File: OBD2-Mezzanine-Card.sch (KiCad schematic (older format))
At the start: 59 parts, among them P1 CONN_02X20

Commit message: sch: Add the 12volt power supply
Also rearrange a bit more

Signed-off-by: Alistair Francis <alistair@alistair23.me>
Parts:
- added D?: D, symbol D
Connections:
- net labels added: V12
- net labels removed: +12V
- wire segments 185 -> 183
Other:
- moved on the sheet: C?, LD?, R?, U?
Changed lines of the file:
@@
 L MCP2561-E/P U?
 U 1 1 5AA61DC4
-P 2150 5450
-F 0 "U?" H 1750 5800 50  0000 L CNN
-F 1 "MCP2561-E/P" H 2250 5800 50  0000 L CNN
-F 2 "Housings_DIP:DIP-8_W7.62mm" H 2150 4950 50  0001 C CIN
-F 3 "" H 2150 5450 50  0001 C CNN
-	1    2150 5450
-	1    0    0    -1
-$EndComp
-Text GLabel 1650 5350 0    60   Input ~ 0
+P 2150 5050
+F 0 "U?" H 1750 5400 50  0000 L CNN
+F 1 "MCP2561-E/P" H 2250 5400 50  0000 L CNN
+F 2 "Housings_DIP:DIP-8_W7.62mm" H 2150 4550 50  0001 C CIN
+F 3 "" H 2150 5050 50  0001 C CNN
+	1    2150 5050
+	1    0    0    -1
+$EndComp
+Text GLabel 1650 4950 0    60   Input ~ 0
 CAN_RX
 Text GLabel 8500 2350 2    60   Input ~ 0
@@
 Text GLabel 8500 2450 2    60   Input ~ 0
 CAN_TX
-Text GLabel 1650 5250 0    60   Input ~ 0
+Text GLabel 1650 4850 0    60   Input ~ 0
 CAN_TX
 $Comp
 L GND #PWR?
 U 1 1 5AA5FF31
-P 2150 5850
-F 0 "#PWR?" H 2150 5600 50  0001 C CNN
-F 1 "GND" H 2150 5700 50  0000 C CNN
-F 2 "" H 2150 5850 50  0001 C CNN
-F 3 "" H 2150 5850 50  0001 C CNN
-	1    2150 5850
+P 2150 5450
+F 0 "#PWR?" H 2150 5200 50  0001 C CNN
+F 1 "GND" H 2150 5300 50  0000 C CNN
+F 2 "" H 2150 5450 50  0001 C CNN
+F 3 "" H 2150 5450 50  0001 C CNN
+	1    2150 5450
 	1    0    0    -1
 $EndComp
@@
 L +5V #PWR?
 U 1 1 5AA5FFA4
-P 1650 4300
-F 0 "#PWR?" H 1650 4150 50  0001 C CNN
-F 1 "+5V" H 1650 4440 50  0000 C CNN
-F 2 "" H 1650 4300 50  0001 C CNN
-F 3 "" H 1650 4300 50  0001 C CNN
-	1    1650 4300
+P 1650 3900
+F 0 "#PWR?" H 1650 3750 50  0001 C CNN
+F 1 "+5V" H 1650 4040 50  0000 C CNN
+F 2 "" H 1650 3900 50  0001 C CNN
+F 3 "" H 1650 3900 50  0001 C CNN
+	1    1650 3900
 	1    0    0    -1
 $EndComp
@@
 L CP1_Small C?
 U 1 1 5AA5FFD8
-P 1650 4600
-F 0 "C?" H 1660 4670 50  0000 L CNN
-F 1 "0.1uF" H 1660 4520 50  0000 L CNN
-F 2 "" H 1650 4600 50  0001 C CNN
-F 3 "" H 1650 4600 50  0001 C CNN
-	1    1650 4600
+P 1650 4200
+F 0 "C?" H 1660 4270 50  0000 L CNN
+F 1 "0.1uF" H 1660 4120 50  0000 L CNN
+F 2 "" H 1650 4200 50  0001 C CNN
+F 3 "" H 1650 4200 50  0001 C CNN
+	1    1650 4200
 	1    0    0    -1
 $EndComp
@@
 L GND #PWR?
 U 1 1 5AA600BE
-P 1650 4750
-F 0 "#PWR?" H 1650 4500 50  0001 C CNN
-F 1 "GND" H 1650 4600 50  0000 C CNN
-F 2 "" H 1650 4750 50  0001 C CNN
-F 3 "" H 1650 4750 50  0001 C CNN
-	1    1650 4750
+P 1650 4350
+F 0 "#PWR?" H 1650 4100 50  0001 C CNN
+F 1 "GND" H 1650 4200 50  0000 C CNN
+F 2 "" H 1650 4350 50  0001 C CNN
+F 3 "" H 1650 4350 50  0001 C CNN
+	1    1650 4350
 	1    0    0    -1
 $EndComp
@@
 L R R?
 U 1 1 5AA6032D
-P 1450 5850
-F 0 "R?" V 1530 5850 50  0000 C CNN
-F 1 "4.7K" V 1450 5850 50  0000 C CNN
-F 2 "" V 1380 5850 50  0001 C CNN
-F 3 "" H 1450 5850 50  0001 C CNN
-	1    1450 5850
+P 1450 5450
+F 0 "R?" V 1530 5450 50  0000 C CNN
+F 1 "4.7K" V 1450 5450 50  0000 C CNN
+F 2 "" V 1380 5450 50  0001 C CNN
+F 3 "" H 1450 5450 50  0001 C CNN
+	1    1450 5450
 	1    0    0    -1
 $EndComp
 Text GLabel 8500 3150 2    60   Input ~ 0
 PwrCntrl
-Text GLabel 1450 6650 2    60   Input ~ 0
+Text GLabel 1450 6250 2    60   Input ~ 0
 PwrCntrl
-NoConn ~ 2650 5450
+NoConn ~ 2650 5050
 $Comp
 L +5V #PWR?
@@
 L +5V #PWR?
 U 1 1 5AA61B64
-P 1000 5750
-F 0 "#PWR?" H 1000 5600 50  0001 C CNN
-F 1 "+5V" H 1000 5890 50  0000 C CNN
-F 2 "" H 1000 5750 50  0001 C CNN
-F 3 "" H 1000 5750 50  0001 C CNN
-	1    1000 5750
+P 1000 5350
+F 0 "#PWR?" H 1000 5200 50  0001 C CNN
+F 1 "+5V" H 1000 5490 50  0000 C CNN
+F 2 "" H 1000 5350 50  0001 C CNN
+F 3 "" H 1000 5350 50  0001 C CNN
+	1    1000 5350
 	1    0    0    -1
 $EndComp
@@
 L Laserdiode_1C2A LD?
 U 1 1 5AA61B9C
-P 1000 6000
-F 0 "LD?" H 950 6175 50  0000 C CNN
-F 1 "LD_1C2A" H 950 5900 50  0000 C CNN
-F 2 "" H 900 5975 50  0001 C CNN
-F 3 "" H 1030 5800 50  0001 C CNN
-	1    1000 6000
+P 1000 5600
+F 0 "LD?" H 950 5775 50  0000 C CNN
+F 1 "LD_1C2A" H 950 5500 50  0000 C CNN
+F 2 "" H 900 5575 50  0001 C CNN
+F 3 "" H 1030 5400 50  0001 C CNN
+	1    1000 5600
 	0    -1   -1   0
 $EndComp
@@
 L R R?
 U 1 1 5AA63138
-P 1000 6500
-F 0 "R?" V 1080 6500 50  0000 C CNN
-F 1 "470" V 1000 6500 50  0000 C CNN
-F 2 "" V 930 6500 50  0001 C CNN
-F 3 "" H 1000 6500 50  0001 C CNN
-	1    1000 6500
+P 1000 6100
+F 0 "R?" V 1080 6100 50  0000 C CNN
+F 1 "470" V 1000 6100 50  0000 C CNN
+F 2 "" V 930 6100 50  0001 C CNN
+F 3 "" H 1000 6100 50  0001 C CNN
+	1    1000 6100
 	1    0    0    -1
 $EndComp
@@
 L R R?
 U 1 1 5AA9D082
+P 3000 5300
+F 0 "R?" V 3080 5300 50  0000 C CNN
+F 1 "100" V 3000 5300 50  0000 C CNN
+F 2 "" V 2930 5300 50  0001 C CNN
+F 3 "" H 3000 5300 50  0001 C CNN
+	1    3000 5300
+	1    0    0    -1
+$EndComp
+$Comp
+L R R?
+U 1 1 5AA9D0D3
+P 3550 5300
+F 0 "R?" V 3630 5300 50  0000 C CNN
+F 1 "100" V 3550 5300 50  0000 C CNN
+F 2 "" V 3480 5300 50  0001 C CNN
+F 3 "" H 3550 5300 50  0001 C CNN
+	1    3550 5300
+	1    0    0    -1
+$EndComp
+$Comp
+L CP1 C?
+U 1 1 5AA9D1F0
 P 3000 5700
-F 0 "R?" V 3080 5700 50  0000 C CNN
-F 1 "100" V 3000 5700 50  0000 C CNN
-F 2 "" V 2930 5700 50  0001 C CNN
+F 0 "C?" H 3025 5800 50  0000 L CNN
+F 1 "560pF" H 3025 5600 50  0000 L CNN
+F 2 "" H 3000 5700 50  0001 C CNN
 F 3 "" H 3000 5700 50  0001 C CNN
 	1    3000 5700
@@
 $EndComp
 $Comp
-L R R?
-U 1 1 5AA9D0D3
+L CP1 C?
+U 1 1 5AA9D24D
 P 3550 5700
-F 0 "R?" V 3630 5700 50  0000 C CNN
-F 1 "100" V 3550 5700 50  0000 C CNN
-F 2 "" V 3480 5700 50  0001 C CNN
+F 0 "C?" H 3575 5800 50  0000 L CNN
+F 1 "560pF" H 3575 5600 50  0000 L CNN
+F 2 "" H 3550 5700 50  0001 C CNN
 F 3 "" H 3550 5700 50  0001 C CNN
 	1    3550 5700
@@
 $EndComp
 $Comp
-L CP1 C?
-U 1 1 5AA9D1F0
-P 3000 6100
-F 0 "C?" H 3025 6200 50  0000 L CNN
-F 1 "560pF" H 3025 6000 50  0000 L CNN
-F 2 "" H 3000 6100 50  0001 C CNN
-F 3 "" H 3000 6100 50  0001 C CNN
-	1    3000 6100
-	1    0    0    -1
-$EndComp
-$Comp
-L CP1 C?
-U 1 1 5AA9D24D
-P 3550 6100
-F 0 "C?" H 3575 6200 50  0000 L CNN
-F 1 "560pF" H 3575 6000 50  0000 L CNN
-F 2 "" H 3550 6100 50  0001 C CNN
-F 3 "" H 3550 6100 50  0001 C CNN
-	1    3550 6100
-	1    0    0    -1
-$EndComp
-$Comp
 L GND #PWR?
 U 1 1 5AA9D388
-P 3000 6350
-F 0 "#PWR?" H 3000 6100 50  0001 C CNN
-F 1 "GND" H 3000 6200 50  0000 C CNN
-F 2 "" H 3000 6350 50  0001 C CNN
-F 3 "" H 3000 6350 50  0001 C CNN
-	1    3000 6350
+P 3000 5950
+F 0 "#PWR?" H 3000 5700 50  0001 C CNN
+F 1 "GND" H 3000 5800 50  0000 C CNN
+F 2 "" H 3000 5950 50  0001 C CNN
+F 3 "" H 3000 5950 50  0001 C CNN
+	1    3000 5950
 	1    0    0    -1
 $EndComp
@@
 L GND #PWR?
 U 1 1 5AA9D3CE
-P 3550 6350
-F 0 "#PWR?" H 3550 6100 50  0001 C CNN
-F 1 "GND" H 3550 6200 50  0000 C CNN
-F 2 "" H 3550 6350 50  0001 C CNN
-F 3 "" H 3550 6350 50  0001 C CNN
-	1    3550 6350
-	1    0    0    -1
-$EndComp
-Text GLabel 3550 5350 2    60   Input ~ 0
+P 3550 5950
+F 0 "#PWR?" H 3550 5700 50  0001 C CNN
+F 1 "GND" H 3550 5800 50  0000 C CNN
+F 2 "" H 3550 5950 50  0001 C CNN
+F 3 "" H 3550 5950 50  0001 C CNN
+	1    3550 5950
+	1    0    0    -1
+$EndComp
+Text GLabel 3550 4950 2    60   Input ~ 0
 CAN_High
-Text GLabel 3000 5550 2    60   Input ~ 0
+Text GLabel 3000 5150 2    60   Input ~ 0
 CAN_Low
 Text GLabel 5750 1100 0    60   Input ~ 0
@@
 F 3 "" H 5200 3600 50  0001 C CNN
 	1    5200 3600
-	1    0    0    -1
-$EndComp
-$Comp
-L +12V #PWR?
-U 1 1 5AA9FA5D
-P 4800 3500
-F 0 "#PWR?" H 4800 3350 50  0001 C CNN
-F 1 "+12V" H 4800 3640 50  0000 C CNN
-F 2 "" H 4800 3500 50  0001 C CNN
-F 3 "" H 4800 3500 50  0001 C CNN
-	1    4800 3500
 	1    0    0    -1
 $EndComp
@@
 Connection ~ 5200 2650
 Wire Wire Line
-	1650 4300 1650 4500
-Wire Wire Line
-	1650 4700 1650 4750
-Wire Wire Line
-	1650 4400 2150 4400
-Wire Wire Line
-	2150 4400 2150 5050
-Connection ~ 1650 4400
-Wire Wire Line
-	1650 5650 1450 5650
-Wire Wire Line
-	1450 5650 1450 5700
+	1650 3900 1650 4100
+Wire Wire Line
+	1650 4300 1650 4350
+Wire Wire Line
+	1650 4000 2150 4000
+Wire Wire Line
+	2150 4000 2150 4650
+Connection ~ 1650 4000
+Wire Wire Line
+	1650 5250 1450 5250
+Wire Wire Line
+	1450 5250 1450 5300
 Wire Wire Line
 	8650 2850 8500 2850
 Wire Wire Line
-	1000 5750 1000 5800
-Wire Wire Line
-	1000 6300 1000 6350
-Wire Wire Line
-	1000 6650 1450 6650
-Wire Wire Line
-	1450 6650 1450 6000
+	1000 5350 1000 5400
+Wire Wire Line
+	1000 5900 1000 5950
+Wire Wire Line
+	1000 6250 1450 6250
+Wire Wire Line
+	1450 6250 1450 5600
 Wire Wire Line
 	4050 2000 4150 2000
@@
 Connection ~ 4150 2200
 Wire Wire Line
-	3000 6250 3000 6350
-Wire Wire Line
-	3550 6350 3550 6250
+	3000 5850 3000 5950
 Wire Wire Line
 	3550 5950 3550 5850
 Wire Wire Line
-	3000 5850 3000 5950
-Wire Wire Line
-	2650 5350 3550 5350
-Wire Wire Line
-	3550 5350 3550 5550
-Wire Wire Line
-	3000 5550 2650 5550
+	3550 5550 3550 5450
+Wire Wire Line
+	3000 5450 3000 5550
+Wire Wire Line
+	2650 4950 3550 4950
+Wire Wire Line
+	3550 4950 3550 5150
+Wire Wire Line
+	3000 5150 2650 5150
 Wire Wire Line
 	5750 1100 5800 1100
@@
 Wire Wire Line
 	5200 4100 5750 4100
-Wire Wire Line
-	4800 3500 4800 3600
-Wire Wire Line
-	4800 3600 4900 3600
 Wire Wire Line
 	5650 3600 5500 3600
@@
 	1    0    0    -1
 $EndComp
+$Comp
+L D D?
+U 1 1 5AAB8BB2
+P 7300 1000
+F 0 "D?" H 7300 1100 50  0000 C CNN
+F 1 "D" H 7300 900 50  0000 C CNN
+F 2 "" H 7300 1000 50  0001 C CNN
+F 3 "" H 7300 1000 50  0001 C CNN
+	1    7300 1000
+	-1   0    0    1
+$EndComp
+Text GLabel 7150 1000 0    60   Input ~ 0
+Vbat
+Text GLabel 7450 1000 2    60   Input ~ 0
+V12
+Text GLabel 4900 3600 0    60   Input ~ 0
+V12
 $EndSCHEMATC

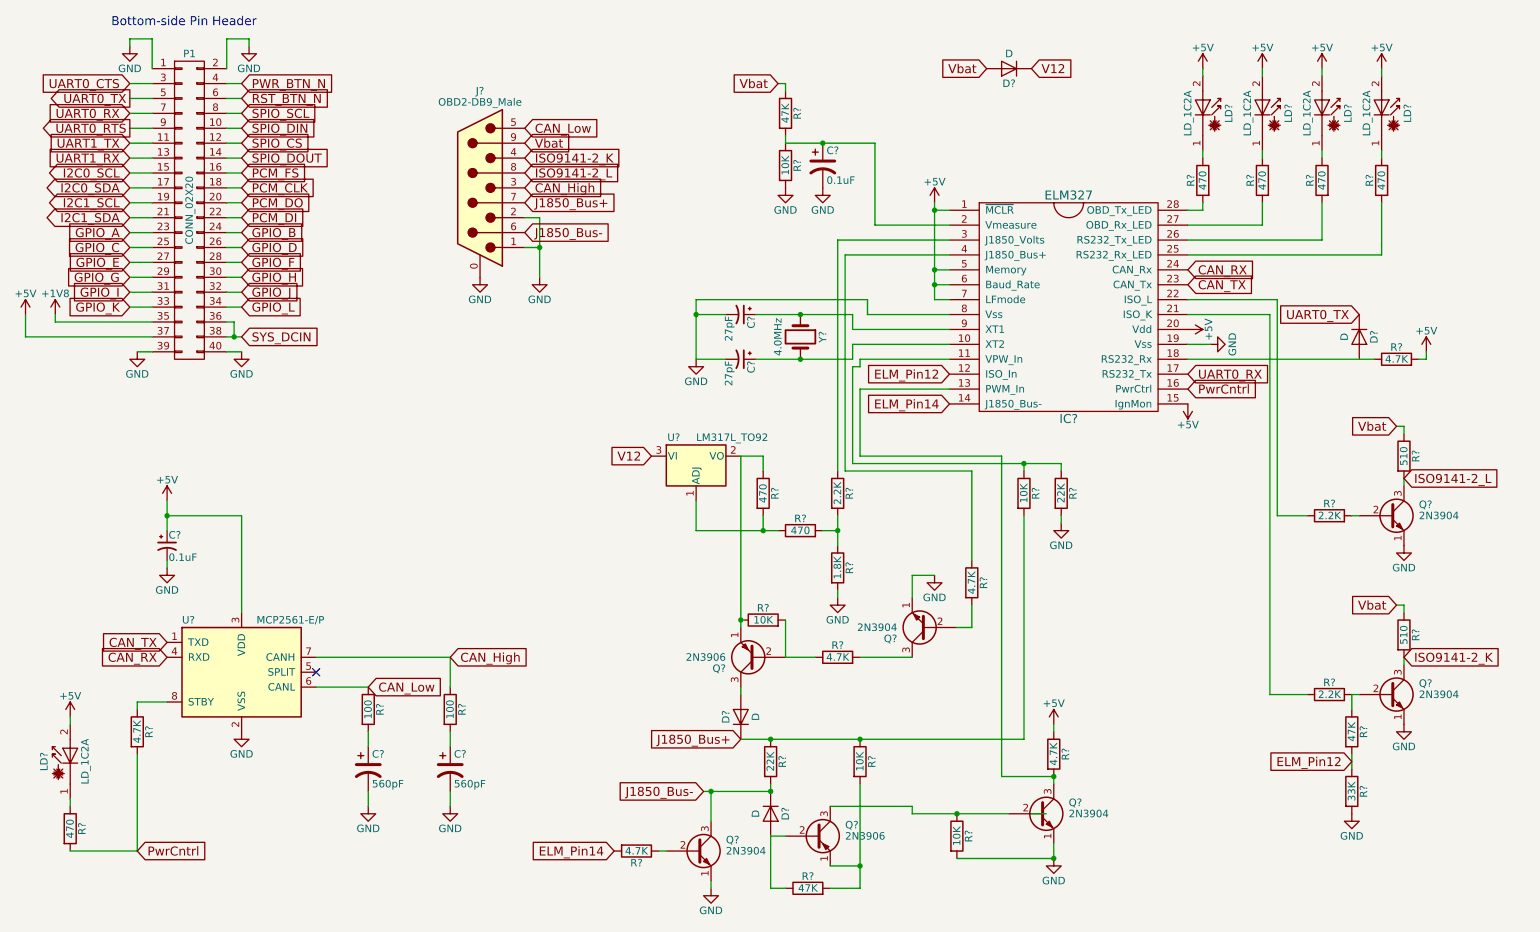
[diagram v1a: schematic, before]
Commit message: sch: Add annotations
Signed-off-by: Alistair Francis <alistair@alistair23.me>
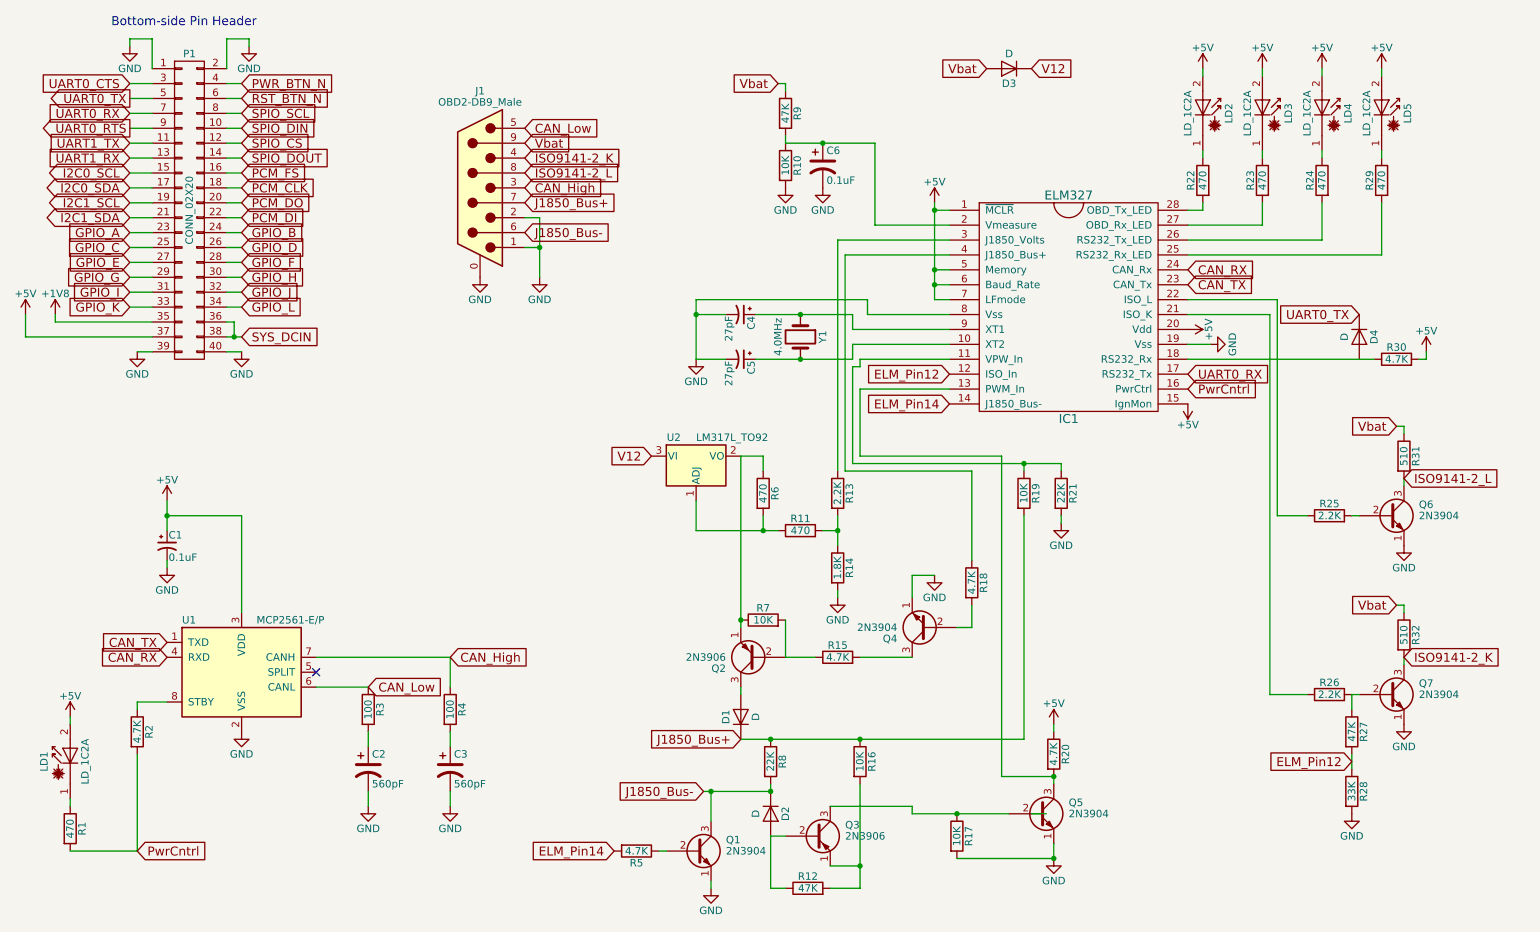
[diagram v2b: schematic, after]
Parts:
- gave numbers to parts that had none: 59

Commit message: sch: Misc fixes to try to fix electrical checks
Signed-off-by: Alistair Francis <alistair@alistair23.me>
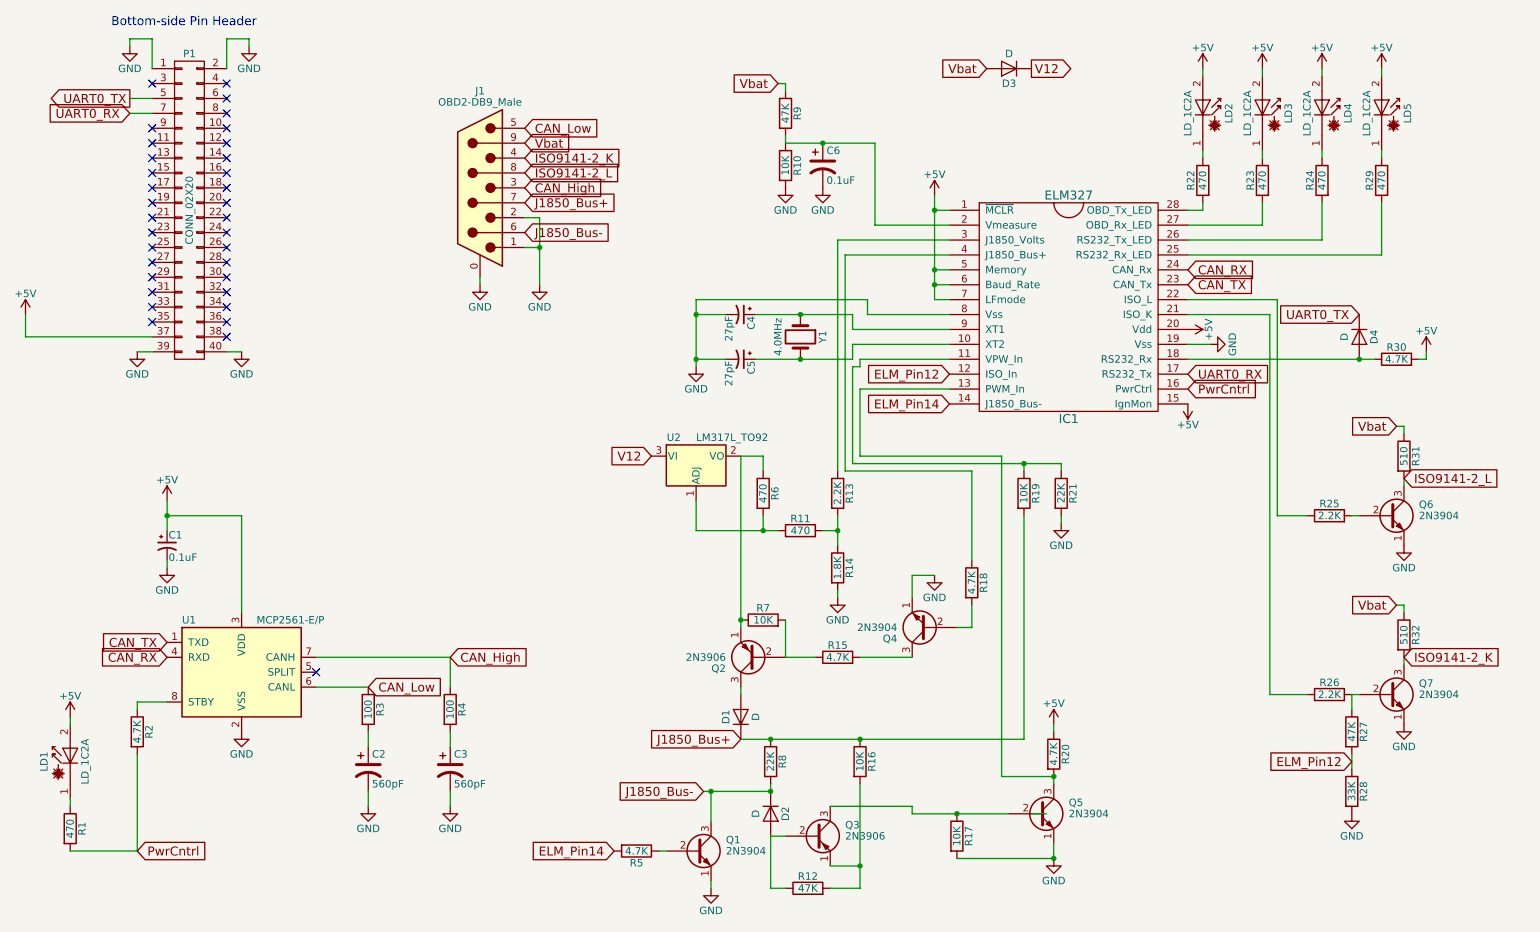
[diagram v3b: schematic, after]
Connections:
- net at IC1.18 (RS232_Rx), R30.1: now also D4.2 (A)
- net +1V8: no longer names the net of P1.35 (P35)
- net GPIO_A: no longer names the net of P1.23 (P23)
- net GPIO_B: no longer names the net of P1.24 (P24)
- net GPIO_C: no longer names the net of P1.25 (P25)
- net GPIO_D: no longer names the net of P1.26 (P26)
- net GPIO_E: no longer names the net of P1.27 (P27)
- net GPIO_F: no longer names the net of P1.28 (P28)
- net GPIO_G: no longer names the net of P1.29 (P29)
- net GPIO_H: no longer names the net of P1.30 (P30)
- net GPIO_I: no longer names the net of P1.31 (P31)
- net GPIO_J: no longer names the net of P1.32 (P32)
- net GPIO_K: no longer names the net of P1.33 (P33)
- net GPIO_L: no longer names the net of P1.34 (P34)
- net I2C0_SCL: no longer names the net of P1.15 (P15)
- net I2C0_SDA: no longer names the net of P1.17 (P17)
- net I2C1_SCL: no longer names the net of P1.19 (P19)
- net I2C1_SDA: no longer names the net of P1.21 (P21)
- net PCM_CLK: no longer names the net of P1.18 (P18)
- net PCM_DI: no longer names the net of P1.22 (P22)
- net PCM_DO: no longer names the net of P1.20 (P20)
- net PCM_FS: no longer names the net of P1.16 (P16)
- net PWR_BTN_N: no longer names the net of P1.4 (P4)
- net RST_BTN_N: no longer names the net of P1.6 (P6)
- net SPIO_CS: no longer names the net of P1.12 (P12)
- net SPIO_DIN: no longer names the net of P1.10 (P10)
- net SPIO_DOUT: no longer names the net of P1.14 (P14)
- net SPIO_SCL: no longer names the net of P1.8 (P8)
- net SYS_DCIN: no longer names the net of P1.36 (P36)
- net SYS_DCIN: no longer P1.38 (P38)
- net UART0_CTS: no longer names the net of P1.3 (P3)
- net UART0_RTS: no longer names the net of P1.9 (P9)
- net UART1_RX: no longer names the net of P1.13 (P13)
- net UART1_TX: no longer names the net of P1.11 (P11)
- no-connect marks 1 -> 34
